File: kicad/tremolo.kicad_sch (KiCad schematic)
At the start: 18 parts, among them IC2 TL072CP

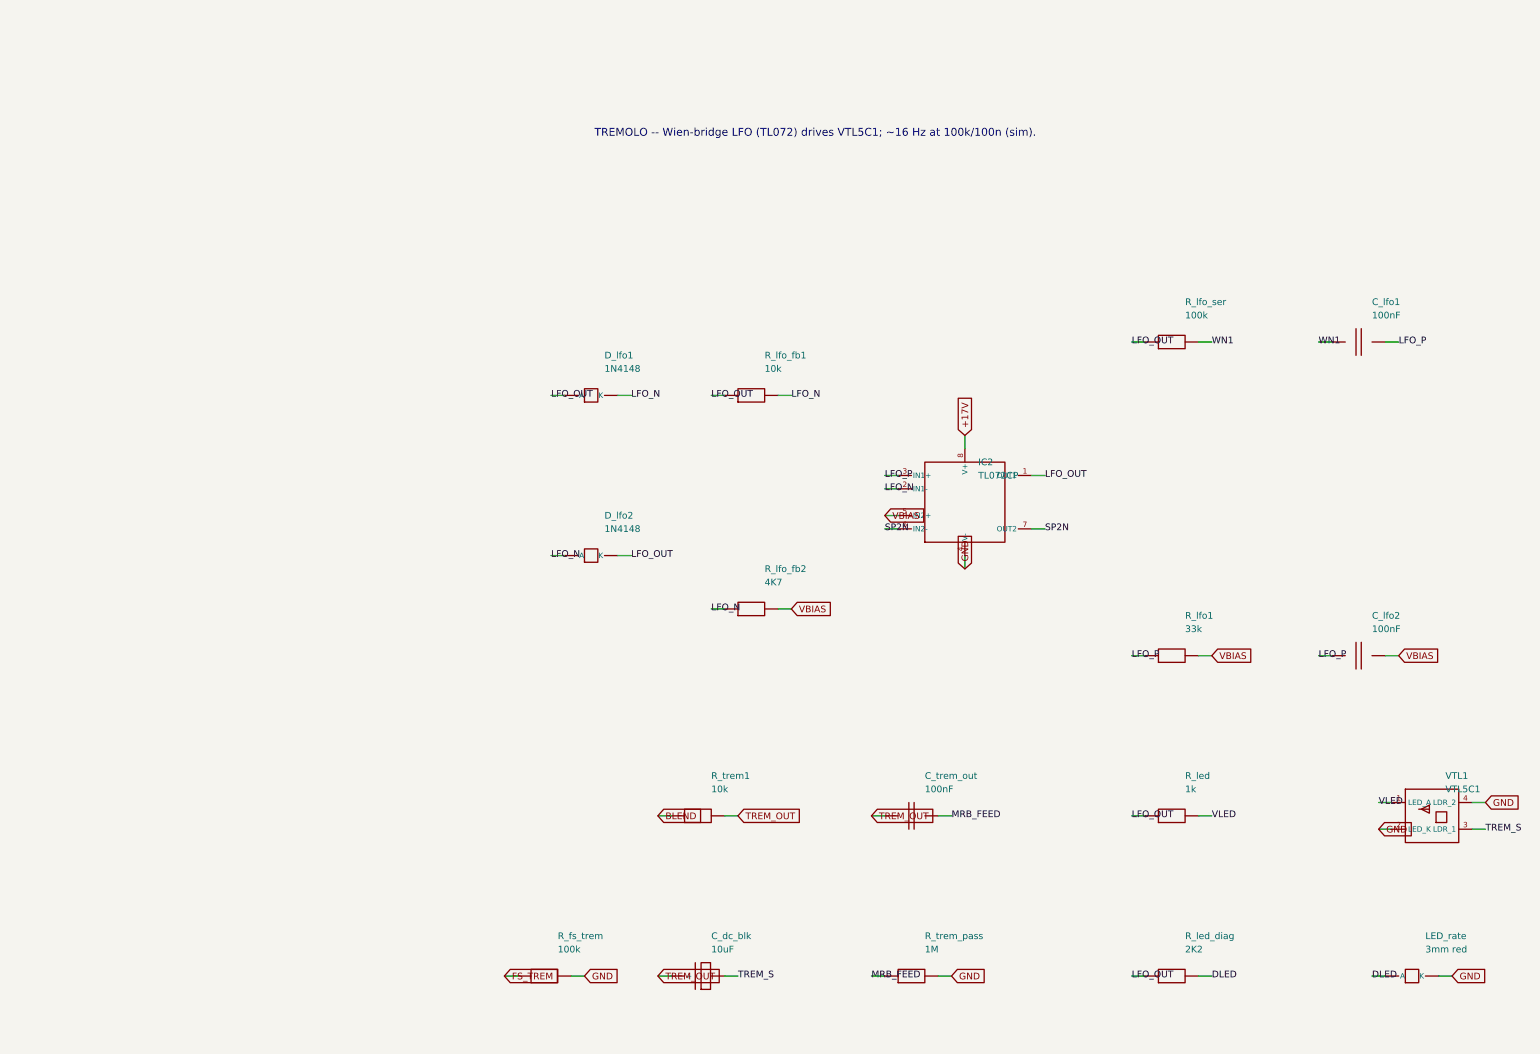
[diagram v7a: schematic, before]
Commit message: Redesign effects chain: active reverb summer + output buffer + split bias
Resolves roast R3 (broken passive mixer) and R6 (shared VBIAS bleed), using the
two spare TL072 halves and verifying with a rail-aware SPICE model.

- Reverb wet/dry mix is now an ACTIVE inverting summer on IC1-B (dry always on,
  wet via POT_REV, unity each, low-Z out about VBIAS_R). Removed the broken
  passive R_dry_tap/R_blend1/R_blend2 (1M dry series made it ~all-wet into an
  unbuffered 110k node).
- IC2-B repurposed as the post-MRB OUTPUT BUFFER driving PA_IN (removed the
  unbuffered R_painput 1M and a dead C_trem_out/R_trem_pass branch).
- VBIAS split into independent VBIAS_R (reverb) and VBIAS_T (tremolo) dividers
  (100k/100k + 47uF each) -> the LFO can no longer modulate the reverb reference.

Verification: new models/opamp_rail.sub clamps the output to the rails (unlike
opamp1p.sub), and spice/tran_reverb_mixer.cir confirms on a single +17V supply:
mid-rail bias 8.50 V, unity (0.0 dB) sum, clips at 15.5/1.5 V -> +-7 V headroom
(~24 dB over a 0.42 V program peak). This is the large-signal/headroom check the
rail-less model could not do (roast R7).

ERC 0; demo DRC 0; full board regenerated (106 footprints); run_all.sh exit 0;
BOM + roast doc + SCHEMATIC-BUILD + spice/README + CHANGELOG updated.

https://claude.ai/code/session_01PkrfUi9tvZfLvudJ7h23qD
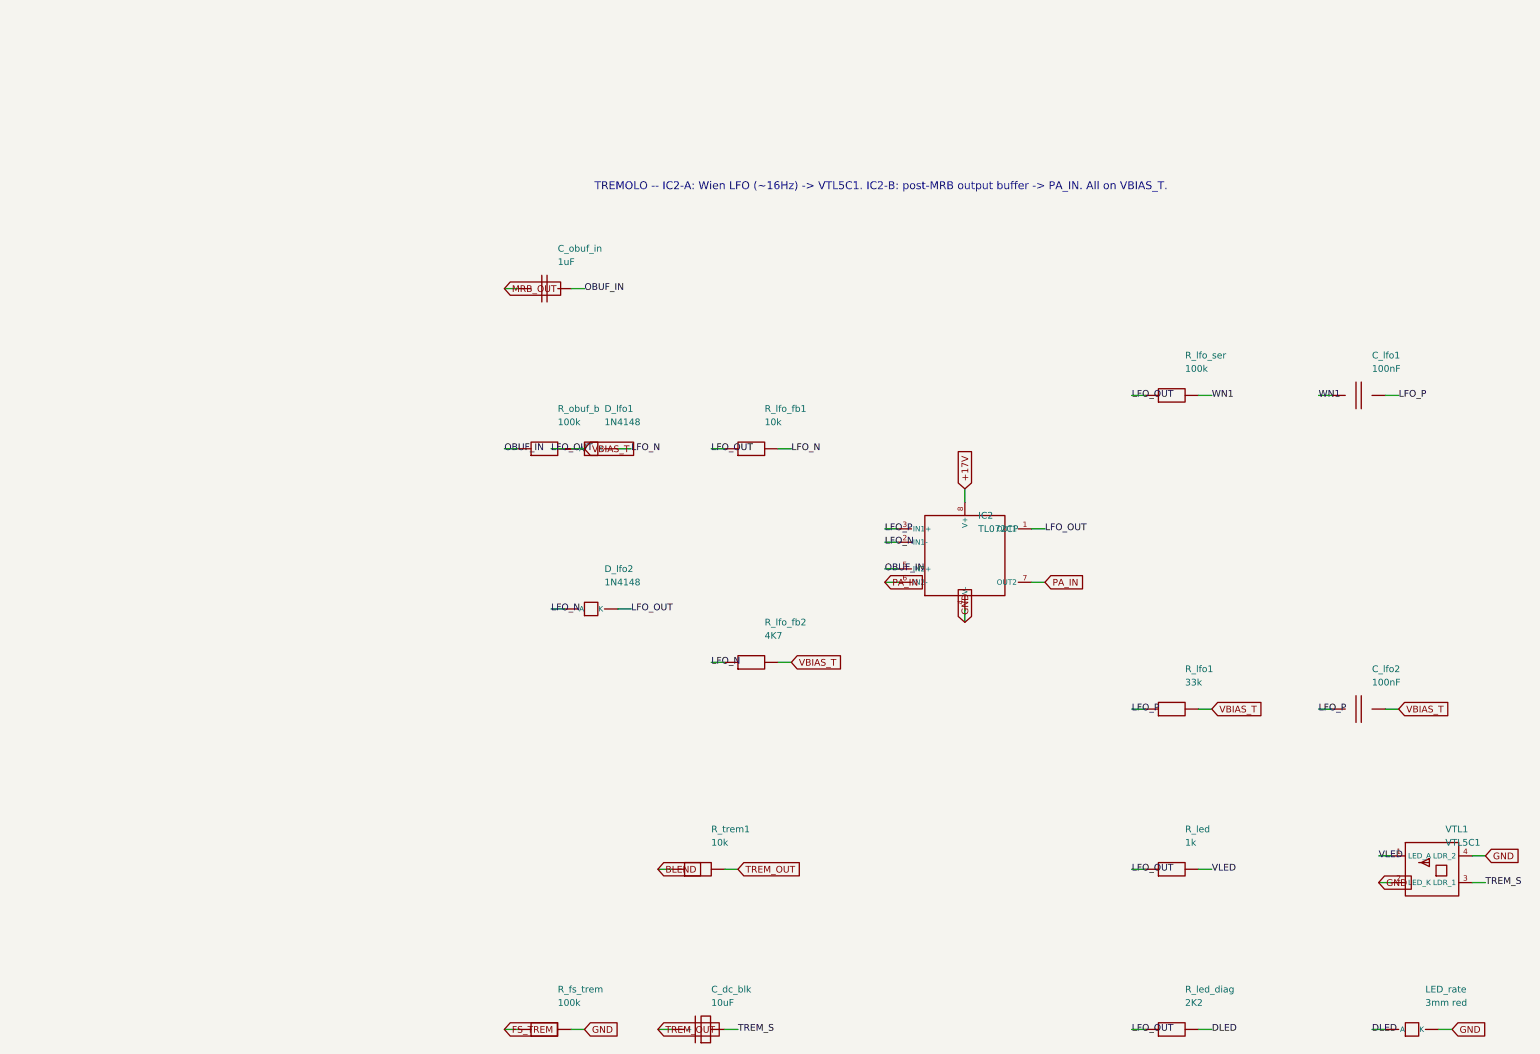
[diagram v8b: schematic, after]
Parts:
- removed C_trem_out: 100nF, Capacitor_THT:C_Disc_D7.5mm_W2.5mm_P5.00mm, symbol cr_primitives:C
- removed R_trem_pass: 1M, Resistor_THT:R_Axial_DIN0207_L6.3mm_D2.5mm_P5.08mm_Vertical, symbol cr_primitives:R
- added C_obuf_in: 1uF, Capacitor_THT:C_Disc_D7.5mm_W2.5mm_P5.00mm, symbol cr_primitives:C
- added R_obuf_b: 100k, Resistor_THT:R_Axial_DIN0207_L6.3mm_D2.5mm_P5.08mm_Vertical, symbol cr_primitives:R
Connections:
- net SP2N renamed PA_IN
- net VBIAS renamed VBIAS_T
- net VBIAS_T: now also R_obuf_b.2; no longer IC2.5 (IN2+)
- new net MRB_OUT: C_obuf_in.1
- new net OBUF_IN: C_obuf_in.2, IC2.5 (IN2+), R_obuf_b.1
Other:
- note added: "TREMOLO -- IC2-A: Wien LFO (~16Hz) -> VTL5C1. IC2-B: post-MRB output buffer -> PA_IN. All on VBIAS_T."
- note removed: "TREMOLO -- Wien-bridge LFO (TL072) drives VTL5C1; ~16 Hz at 100k/100n (sim)."
